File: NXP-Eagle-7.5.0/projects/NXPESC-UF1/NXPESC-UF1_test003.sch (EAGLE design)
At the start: 59 parts, among them J2 FLH1-03SZ-S3A-T, U1 MKV31F512VLL12-M, U10 PSMN1R4-30YLD, U11 PSMN1R4-30YLD, U12 PSMN1R4-30YLD, U13 PSMN1R4-30YLD, U8 PSMN1R4-30YLD, U9 PSMN1R4-30YLD

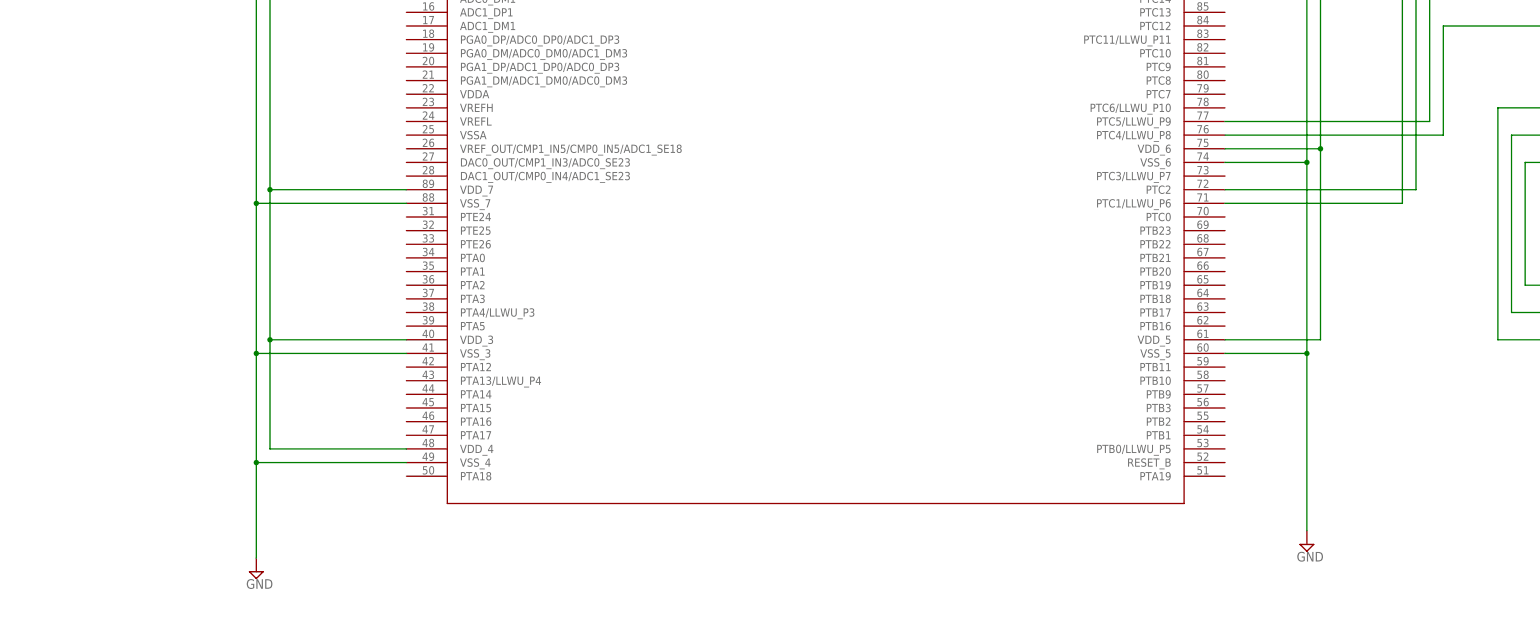
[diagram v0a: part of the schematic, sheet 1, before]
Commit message: Trial placement on board, Note that the schematic is not complete yet. Also created the 64 pin KV 31 Part.
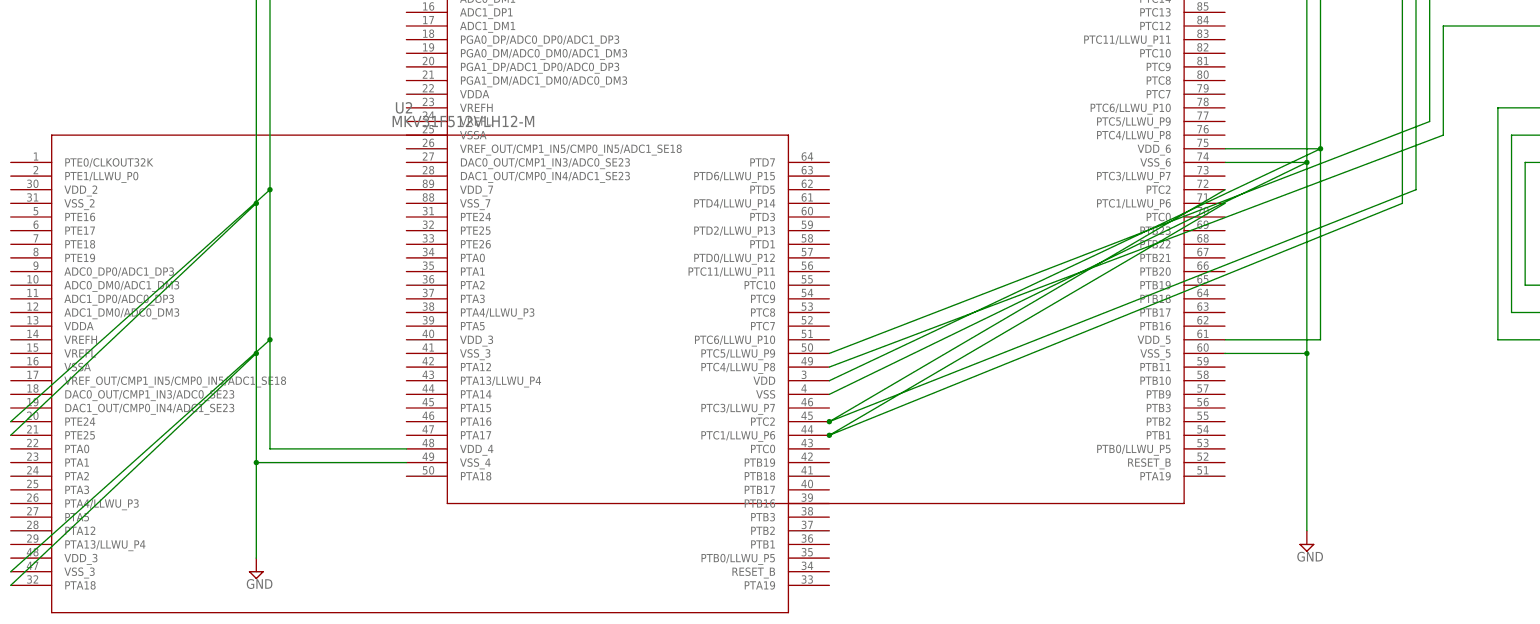
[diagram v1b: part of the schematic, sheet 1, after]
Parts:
- added U2: MKV31F512VLH12-M, MKV31F512VLH12:MKV31F512VLH12-M
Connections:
- net +3V3: now also U2.PTE24, U2.VDD, U2.VSS_3; no longer U1.VDD_3, U1.VDD_7
- net GND: now also U2.PTA18, U2.PTE25, U2.VSS; no longer U1.VSS_3, U1.VSS_7
- net N$5: now also U2.PTC1/LLWU_P6
- net N$6: now also U2.PTC2
- net N$7: now also U2.PTC5/LLWU_P9; no longer U1.PTC5/LLWU_P9
- net N$8: now also U2.PTC4/LLWU_P8; no longer U1.PTC4/LLWU_P8

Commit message: Working on Layout trying to arrange drivers fets and opamps
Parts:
- added H1: DNI(HDR-TSHSM-5-05-D-02-G-V-XXX-TB-0-LF), etc-connector-002a:HDR-TSHSM-5-05-D-02-G-V-XXX-TB-0-LF
- added H3: TC2050-IDCNH, etc-connector-003a:TC2050-IDCNH
- added R39: RESC0603-4K7-5, etc_rcl:RESC0603-4K7-5
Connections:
- net N$15 renamed CS_DCB_H
- net N$16 renamed CS_DCB_L
- removed net CA_A_L: R14.2
- removed net VDD: C1.+, U$1.VDD
- new net N$15: H1.7, H3.TCK
- new net N$16: H1.8, H3.NOTUSED@1
- new net N$18: H1.9, H3.GND/+5V
- new net RESET_B: H1.10, H3.TDO, U2.RESET_B
- new net SWD_CLK: H1.4, H3.NOTUSED@2, U2.PTA0
- new net SWD_DIO: H1.2, H3.RESET, R39.1, U2.PTA3
- new net TRACE_SWO: H1.6, H3.TDI, U2.PTA2
- net +3V3: now also C1.+, H1.1, H3.VCC, R39.2, U$1.VDD
- net CS_A_L: now also R14.2
- net GND: now also H1.3, H1.5, H3.GND, H3.TMS
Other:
- note added: "10 pin JTAG"
- note added: "JTAG Connector"

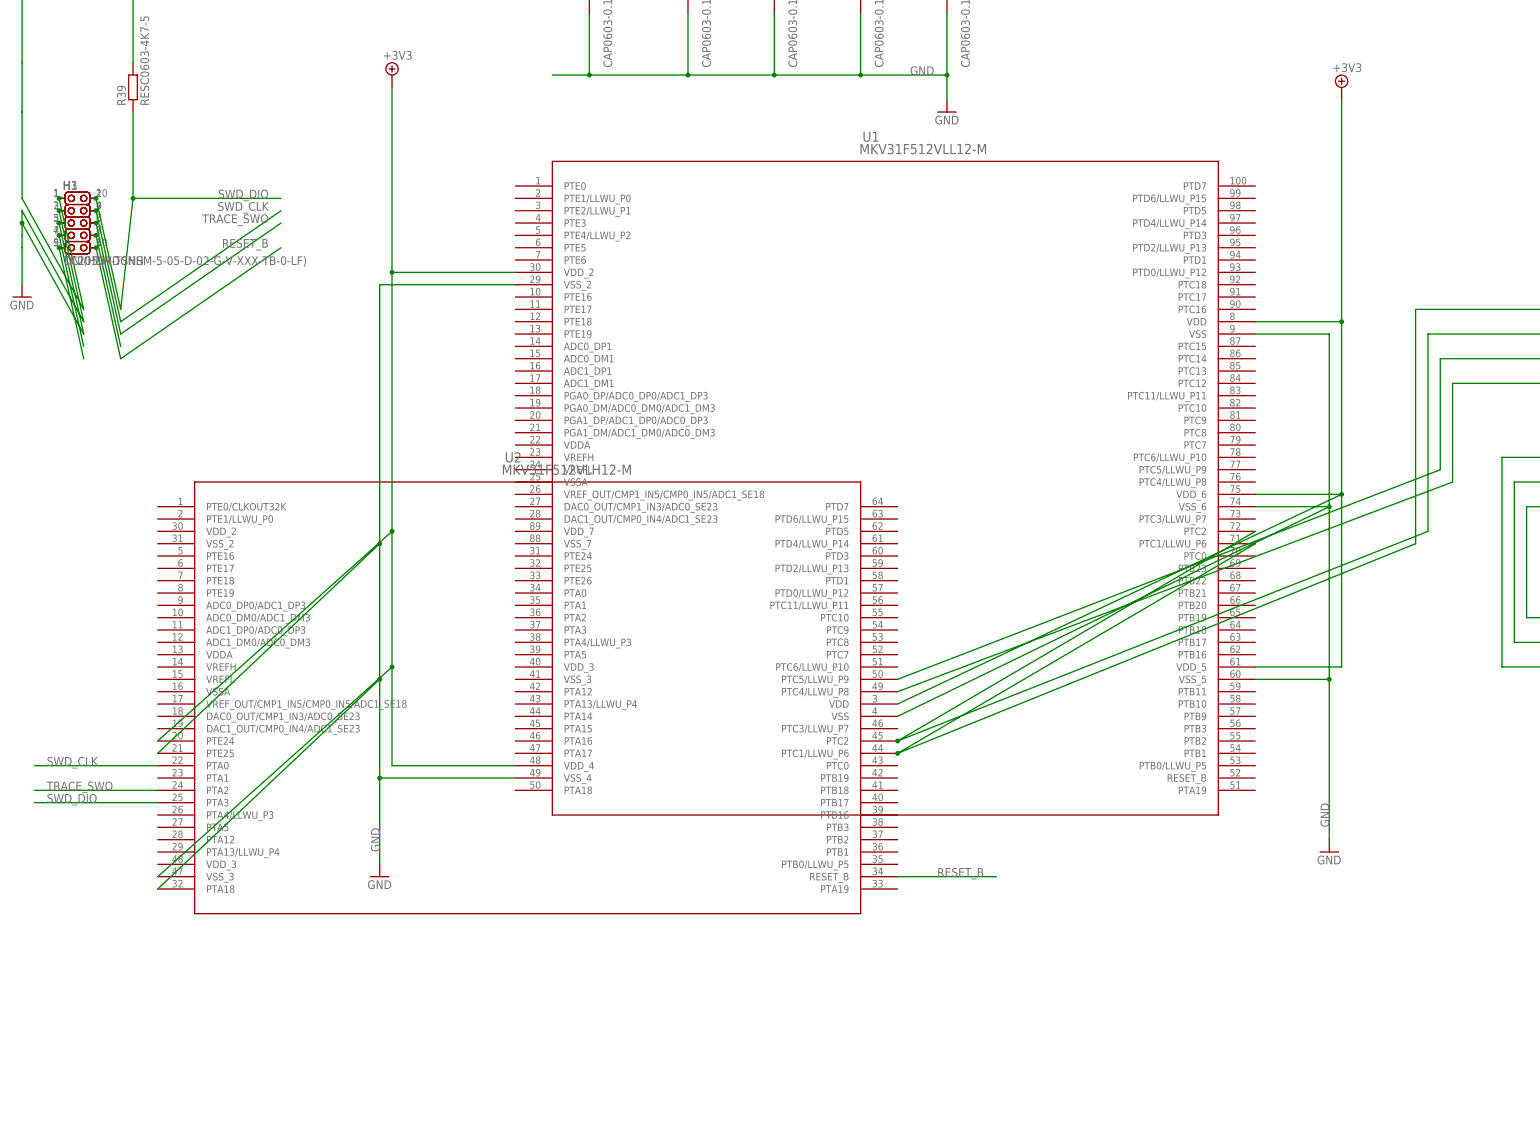
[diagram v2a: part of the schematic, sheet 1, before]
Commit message: Add PHY and DF13 4-pin CAN conn to SCH
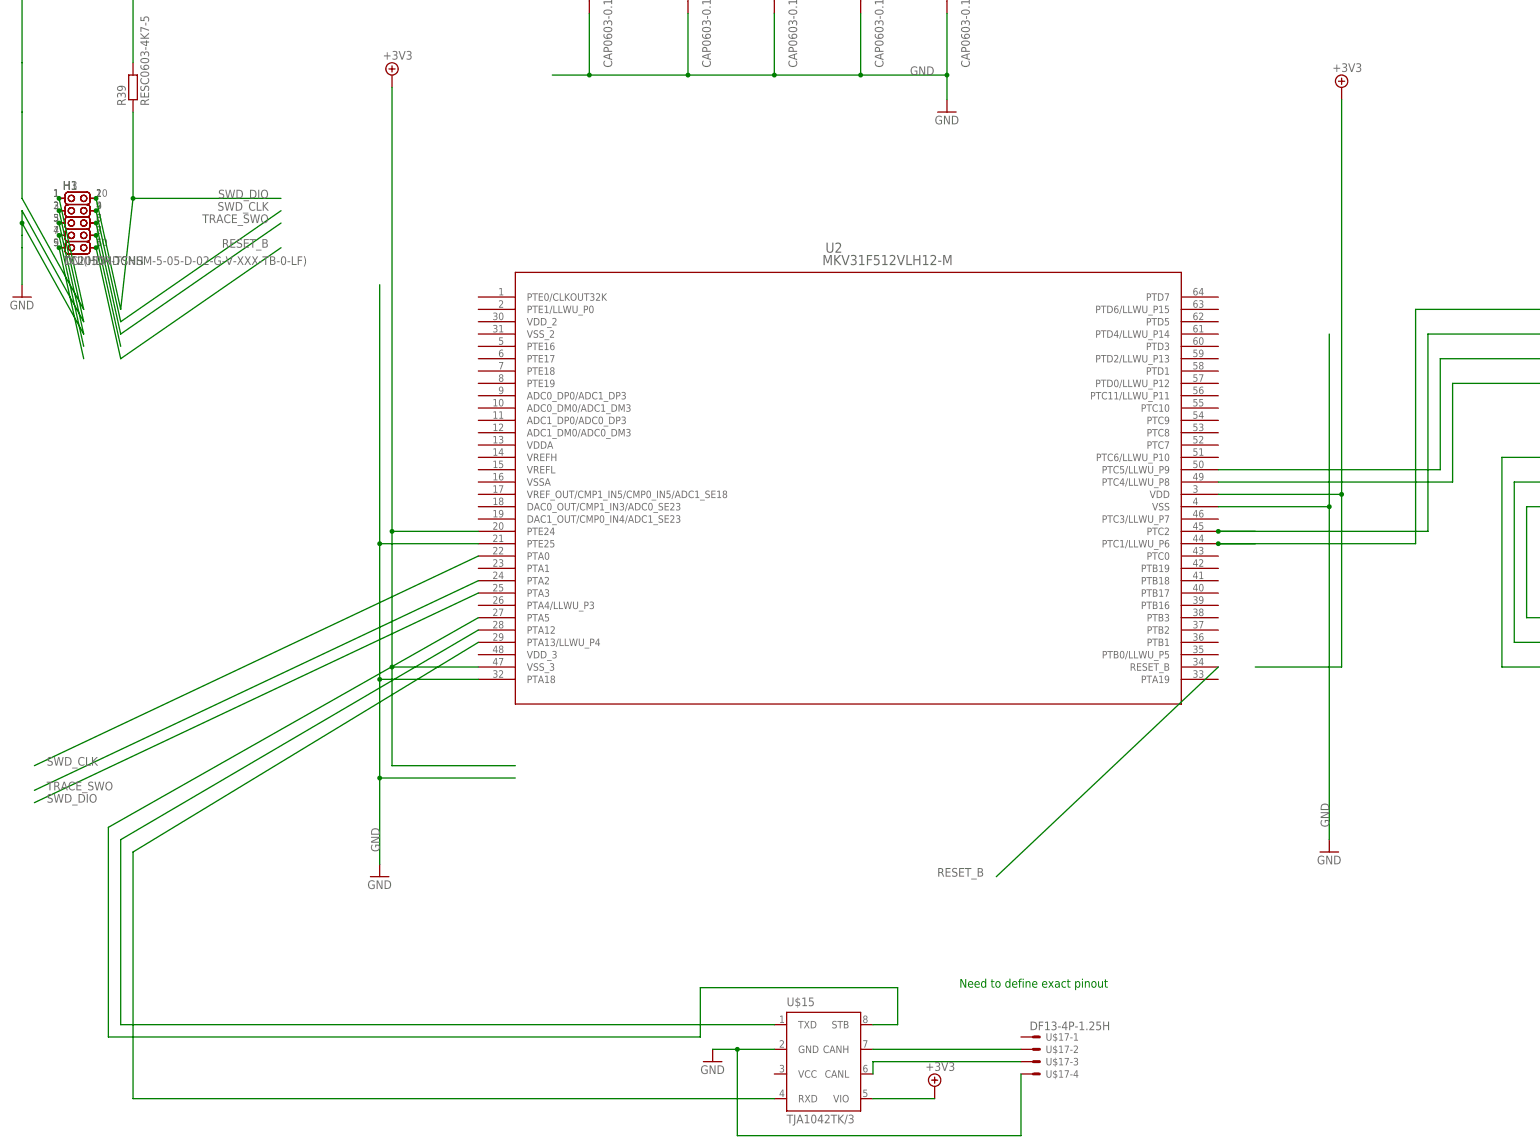
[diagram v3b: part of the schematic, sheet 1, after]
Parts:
- removed U1: MKV31F512VLL12-M, MKV31F512VLL12:MKV31F512VLL12-M
- added U$15: TJA1042TK/3, TJA1042T:TJA1042TK/3
- added U$17: DF13-4P-1.25H, pixhawk2:DF13-4P-1.25H
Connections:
- new net CAN0_RX: U$15.RXD, U2.PTA13/LLWU_P4
- new net CAN0_TX: U$15.TXD, U2.PTA12
- new net N$22: U$15.CANH, U$17-2.S
- new net N$23: U$15.CANL, U$17-3.S
- new net STB: U$15.STB, U2.PTA5
- net +3V3: now also U$15.VIO; no longer U1.VDD, U1.VDD_2, U1.VDD_4, U1.VDD_5, U1.VDD_6
- net GND: now also U$15.GND, U$17-4.S; no longer U1.VSS, U1.VSS_2, U1.VSS_4, U1.VSS_5, U1.VSS_6
- net N$5: no longer U1.PTC1/LLWU_P6
- net N$6: no longer U1.PTC2
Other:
- note added: "Need to define exact pinout"
- moved on the sheet: U2
